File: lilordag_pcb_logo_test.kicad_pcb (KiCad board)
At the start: 2 copper layers, 98.1 x 100 mm, 124 parts, among them J1 USB4105-GF-A, Q1 MMBT3906, Q2 BC846, Q3 MMBT3906, Q4 BC846, Q5 BC846, Q6 BC846, SW1 PCM12SMTR

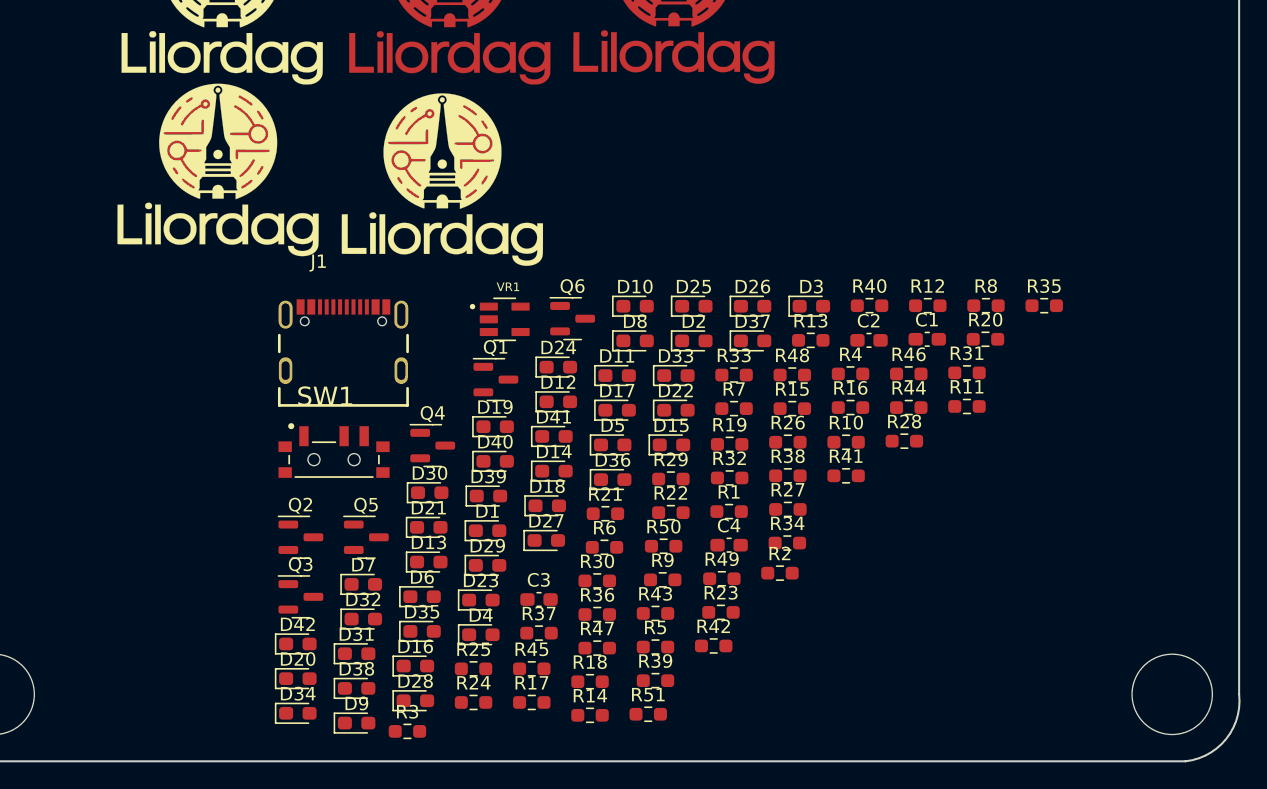
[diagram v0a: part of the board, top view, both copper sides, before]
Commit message: Added 2 CR2032 battery holders.
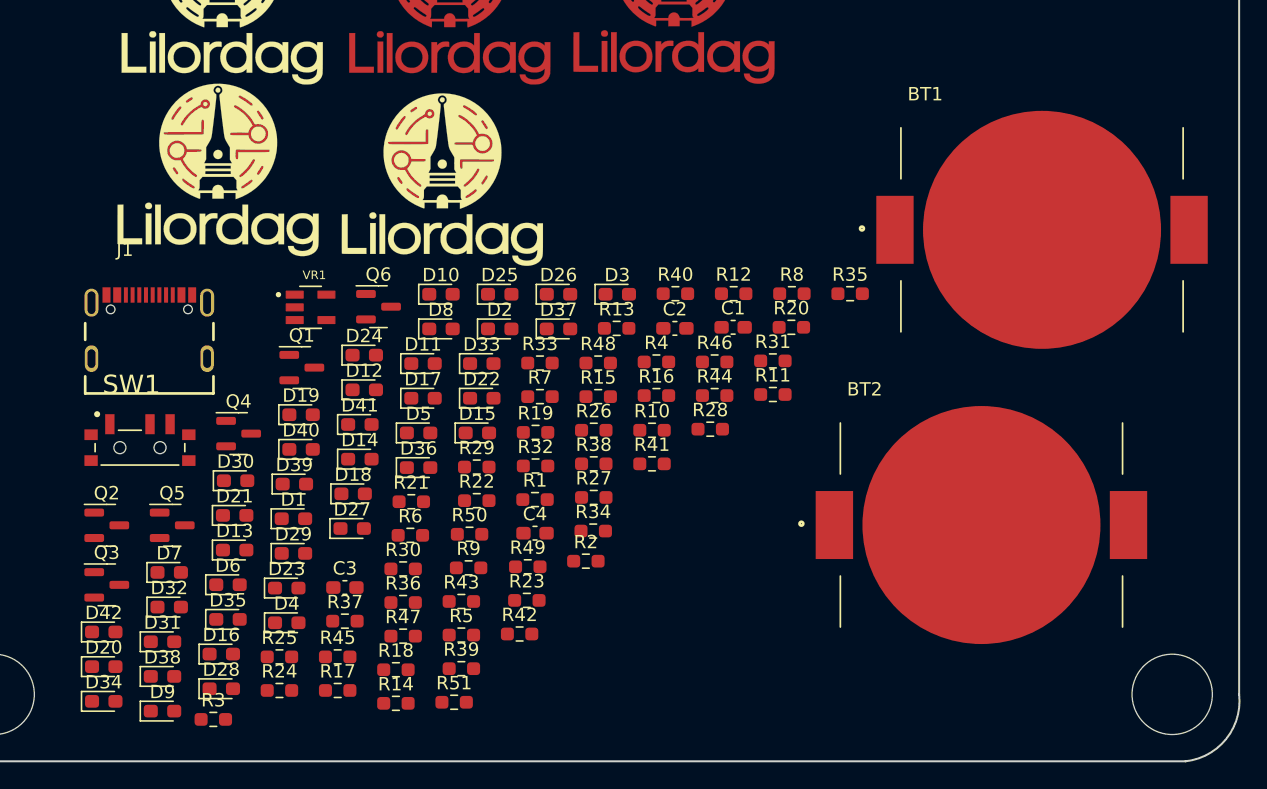
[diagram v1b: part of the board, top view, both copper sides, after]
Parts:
- added BT1: BK-912-TR, BK-912-TR-batt-holder:MPD_BK-912-TR, F.Cu at (111.3, 90.3)
- added BT2: BK-912-TR, BK-912-TR-batt-holder:MPD_BK-912-TR, F.Cu at (106.8, 112.3)
- moved D1 14.5 mm to (55.4, 111.9)
- moved D23 14.5 mm to (54.9, 117.1)
- moved D27 14.5 mm to (59.7, 112.6)
- moved D29 14.5 mm to (55.4, 114.5)
- moved D4 14.5 mm to (54.9, 119.7)
- moved Q1 14.5 mm to (56.0, 100.6)
- moved Q4 14.5 mm to (51.3, 105.5)
- moved R14 14.5 mm to (63.0, 125.7)
- moved R18 14.5 mm to (63.0, 123.2)
- moved VR1 14.5 mm to (56.6, 96.1)
- moved C1 14.5 mm to (88.2, 97.6)
- moved C2 14.5 mm to (83.8, 97.7)
- moved C3 14.5 mm to (59.2, 117.0)
- moved C4 14.5 mm to (73.4, 113.0)
- moved D10 14.5 mm to (66.4, 95.1)
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
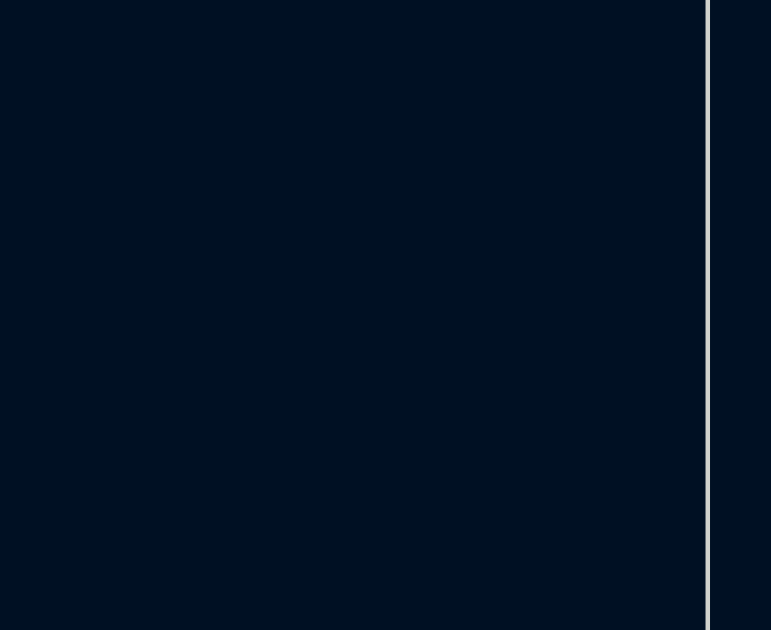
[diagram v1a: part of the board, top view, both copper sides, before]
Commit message: Added the protection circuit to the PCB.
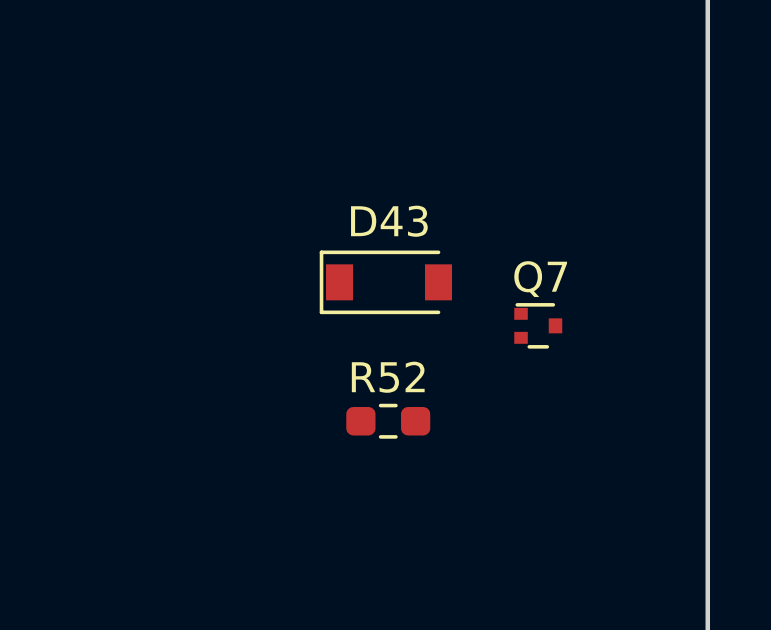
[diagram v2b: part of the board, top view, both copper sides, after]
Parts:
- added D43: MMSZ5233B 6V, Diode_SMD:D_SOD-123, F.Cu at (115.4, 65.8)
- added Q7: SSM3J56MFV, Package_TO_SOT_SMD:SOT-723, F.Cu at (120.3, 67.2)
- added R52: 100k, Resistor_SMD:R_0603_1608Metric_Pad0.98x0.95mm_HandSolder, F.Cu at (115.3, 70.4)

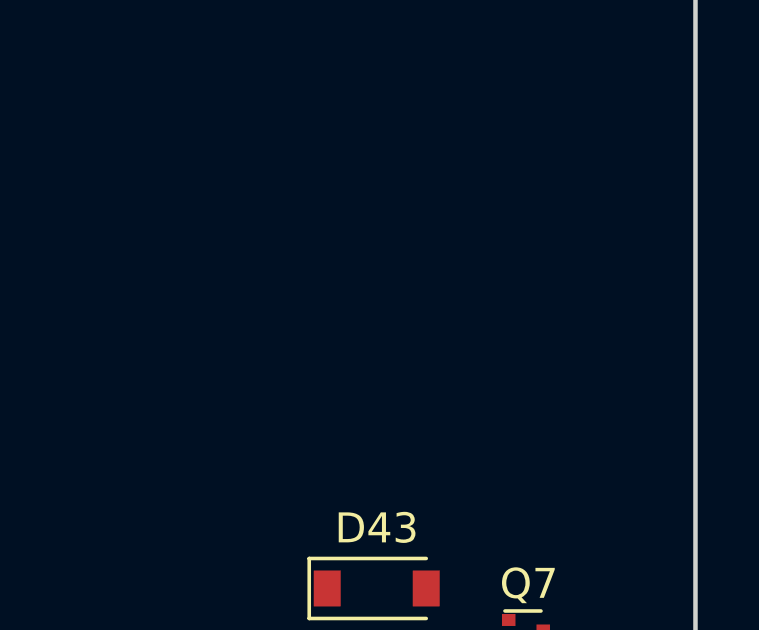
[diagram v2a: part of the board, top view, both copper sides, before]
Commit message: Added selector between battery and USB.
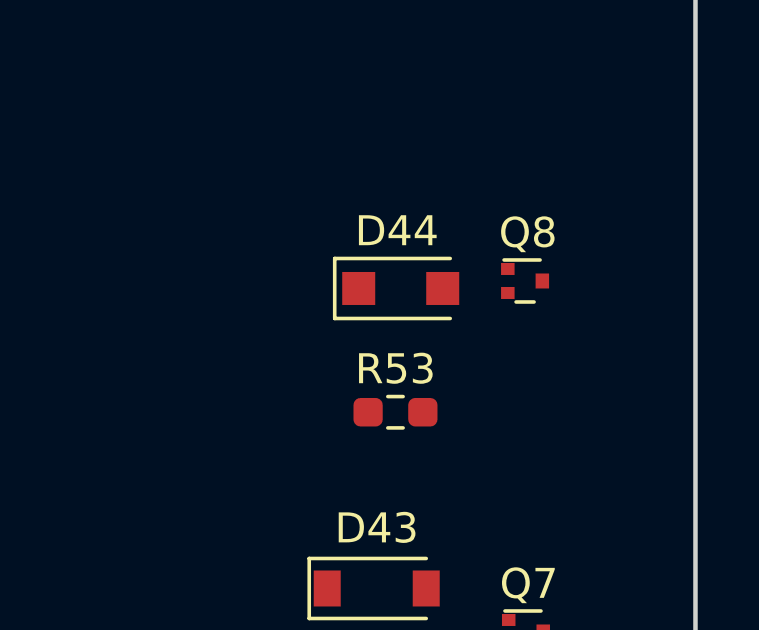
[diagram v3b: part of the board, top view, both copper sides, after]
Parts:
- added D44: D_Schottky, Diode_SMD:D_SOD-123F, F.Cu at (116.2, 55.8)
- added Q8: SSM3J56MFV, Package_TO_SOT_SMD:SOT-723, F.Cu at (120.3, 55.5)
- added R53: 100k, Resistor_SMD:R_0603_1608Metric_Pad0.98x0.95mm_HandSolder, F.Cu at (116.0, 59.9)

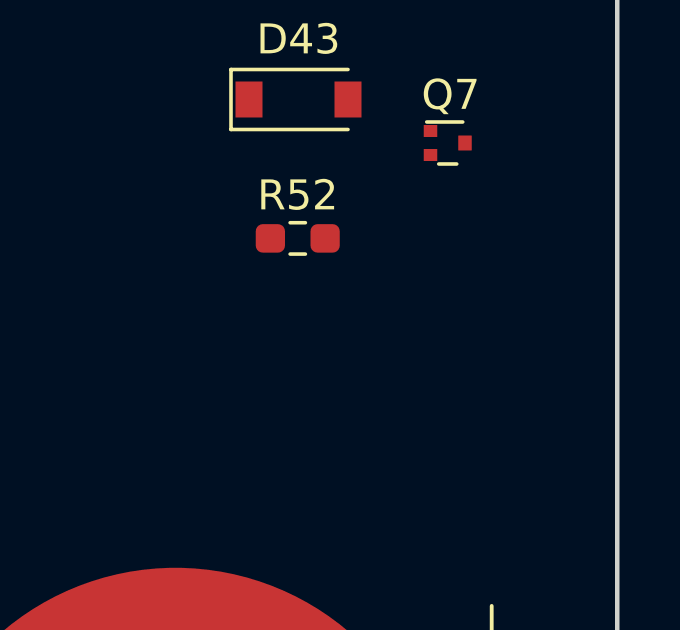
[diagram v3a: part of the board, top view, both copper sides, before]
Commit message: Added an on-off switch to the battery.
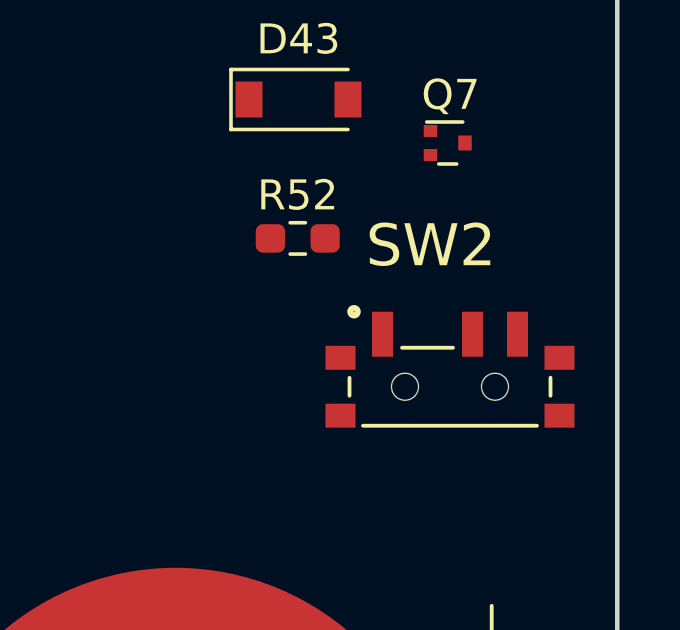
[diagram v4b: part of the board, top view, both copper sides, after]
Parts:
- added SW2: PCM12SMTR, PCM12SMTR:SW_PCM12SMTR, F.Cu at (120.4, 75.4)
- Q1: value MMBT3906 -> BC846
- Q4: value BC846 -> MMBT3906
- R1, R24, R25, R46: value 1k -> 470
- R10, R12, R31, R33: value 470 -> 1k
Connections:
- BT1 pad 1: +BATT -> Net-(BT1-Pad1)
- BT1 pad 2: +BATT -> Net-(BT1-Pad1)
- D1 pad 1: GND -> Net-(D1-Pad1)
- D10 pad 1: GND -> Net-(D10-Pad1)
- D11 pad 1: Net-(D11-Pad1) -> Net-(D1-Pad1)
- D12 pad 1: Net-(D11-Pad1) -> Net-(D10-Pad1)
- D13 pad 1: Net-(D11-Pad1) -> Net-(D1-Pad1)
- D14 pad 1: Net-(D11-Pad1) -> Net-(D10-Pad1)
- D15 pad 1: Net-(D11-Pad1) -> Net-(D1-Pad1)
- D16 pad 1: Net-(D11-Pad1) -> Net-(D10-Pad1)
- D17 pad 1: Net-(D11-Pad1) -> Net-(D1-Pad1)
- D18 pad 1: Net-(D11-Pad1) -> Net-(D10-Pad1)
- D19 pad 1: Net-(D11-Pad1) -> Net-(D1-Pad1)
- D2 pad 1: GND -> Net-(D10-Pad1)
- D20 pad 1: Net-(D11-Pad1) -> Net-(D10-Pad1)
- D21 pad 1: Net-(D21-Pad1) -> GND
- D22 pad 1: Net-(D21-Pad1) -> GND
- D23 pad 1: Net-(D21-Pad1) -> GND
- D24 pad 1: Net-(D21-Pad1) -> GND
- D25 pad 1: Net-(D21-Pad1) -> GND
- D26 pad 1: Net-(D21-Pad1) -> GND
- D27 pad 1: Net-(D21-Pad1) -> GND
- D28 pad 1: Net-(D21-Pad1) -> GND
- D29 pad 1: Net-(D21-Pad1) -> GND
- D3 pad 1: GND -> Net-(D1-Pad1)
- D30 pad 1: Net-(D21-Pad1) -> GND
- D4 pad 1: GND -> Net-(D10-Pad1)
- D5 pad 1: GND -> Net-(D1-Pad1)
- D6 pad 1: GND -> Net-(D10-Pad1)
- D7 pad 1: GND -> Net-(D1-Pad1)
- D8 pad 1: GND -> Net-(D10-Pad1)
- D9 pad 1: GND -> Net-(D1-Pad1)
- Q1 pad 2: +3.3V -> GND
- Q1 pad 3: Net-(Q1-Pad3) -> Net-(D1-Pad1)
- Q2 pad 3: Net-(D11-Pad1) -> Net-(D10-Pad1)
- Q4 pad 2: GND -> +3.3V
- Q4 pad 3: Net-(D21-Pad1) -> Net-(Q4-Pad3)
- R1 pad 1: LEFT_LED_CONNECTION -> +3.3V
- R1 pad 2: Net-(Q1-Pad1) -> Net-(D1-Pad2)
- R10 pad 1: Net-(Q1-Pad3) -> LEFT_LED_CONNECTION
- R10 pad 2: Net-(D7-Pad2) -> Net-(Q1-Pad1)
- R11 pad 1: Net-(Q1-Pad3) -> +3.3V
- R12 pad 1: Net-(Q1-Pad3) -> RIGHT_LED_CONNECTION
- R12 pad 2: Net-(D9-Pad2) -> Net-(Q2-Pad1)
- R13 pad 1: Net-(Q1-Pad3) -> +3.3V
- R13 pad 2: Net-(D10-Pad2) -> Net-(D9-Pad2)
- R14 pad 2: Net-(D11-Pad2) -> Net-(D10-Pad2)
- R15 pad 2: Net-(D12-Pad2) -> Net-(D11-Pad2)
- R16 pad 2: Net-(D13-Pad2) -> Net-(D12-Pad2)
- R17 pad 2: Net-(D14-Pad2) -> Net-(D13-Pad2)
- R18 pad 2: Net-(D15-Pad2) -> Net-(D14-Pad2)
- R19 pad 2: Net-(D16-Pad2) -> Net-(D15-Pad2)
- R20 pad 2: Net-(D17-Pad2) -> Net-(D16-Pad2)
- R21 pad 2: Net-(D18-Pad2) -> Net-(D17-Pad2)
- R22 pad 2: Net-(D19-Pad2) -> Net-(D18-Pad2)
- R23 pad 2: Net-(D20-Pad2) -> Net-(D19-Pad2)
- R24 pad 1: LEFT_LED_CONNECTION -> +3.3V
- R24 pad 2: Net-(Q2-Pad1) -> Net-(D20-Pad2)
- R25 pad 1: RIGHT_LED_CONNECTION -> Net-(Q3-Pad3)
- R25 pad 2: Net-(Q3-Pad1) -> Net-(D21-Pad2)
- R26 pad 1: +3.3V -> Net-(Q4-Pad3)
- R26 pad 2: Net-(D21-Pad2) -> Net-(D22-Pad2)
- R27 pad 1: +3.3V -> Net-(Q3-Pad3)
- R27 pad 2: Net-(D22-Pad2) -> Net-(D23-Pad2)
- R28 pad 1: +3.3V -> Net-(Q4-Pad3)
- R28 pad 2: Net-(D23-Pad2) -> Net-(D24-Pad2)
- R29 pad 1: +3.3V -> Net-(Q3-Pad3)
- R29 pad 2: Net-(D24-Pad2) -> Net-(D25-Pad2)
- R30 pad 1: +3.3V -> Net-(Q4-Pad3)
- R30 pad 2: Net-(D25-Pad2) -> Net-(D26-Pad2)
- R31 pad 1: +3.3V -> LEFT_LED_CONNECTION
- R31 pad 2: Net-(D26-Pad2) -> Net-(Q3-Pad1)
- R32 pad 1: +3.3V -> Net-(Q3-Pad3)
- R33 pad 1: +3.3V -> RIGHT_LED_CONNECTION
- R33 pad 2: Net-(D28-Pad2) -> Net-(Q4-Pad1)
- R34 pad 1: +3.3V -> Net-(Q4-Pad3)
- R34 pad 2: Net-(D29-Pad2) -> Net-(D28-Pad2)
- R35 pad 1: +3.3V -> Net-(Q3-Pad3)
- R35 pad 2: Net-(D30-Pad2) -> Net-(D29-Pad2)
- R36 pad 1: Net-(Q3-Pad3) -> Net-(Q4-Pad3)
- R36 pad 2: Net-(D31-Pad2) -> Net-(D30-Pad2)
- R37 pad 2: Net-(D32-Pad2) -> Net-(D31-Pad2)
- R38 pad 1: Net-(Q3-Pad3) -> Net-(Q4-Pad3)
- R38 pad 2: Net-(D33-Pad2) -> Net-(D32-Pad2)
- R39 pad 2: Net-(D34-Pad2) -> Net-(D33-Pad2)
- R4 pad 1: Net-(Q1-Pad3) -> +3.3V
- R4 pad 2: Net-(D1-Pad2) -> Net-(D2-Pad2)
- R40 pad 1: Net-(Q3-Pad3) -> Net-(Q4-Pad3)
- R40 pad 2: Net-(D35-Pad2) -> Net-(D34-Pad2)
- R41 pad 2: Net-(D36-Pad2) -> Net-(D35-Pad2)
- R42 pad 1: Net-(Q3-Pad3) -> Net-(Q4-Pad3)
- R42 pad 2: Net-(D37-Pad2) -> Net-(D36-Pad2)
- R43 pad 2: Net-(D38-Pad2) -> Net-(D37-Pad2)
- R44 pad 1: Net-(Q3-Pad3) -> Net-(Q4-Pad3)
- R44 pad 2: Net-(D39-Pad2) -> Net-(D38-Pad2)
- R45 pad 2: Net-(D40-Pad2) -> Net-(D39-Pad2)
- R46 pad 1: RIGHT_LED_CONNECTION -> Net-(Q4-Pad3)
- R46 pad 2: Net-(Q4-Pad1) -> Net-(D40-Pad2)
- R5 pad 1: Net-(Q1-Pad3) -> +3.3V
- R5 pad 2: Net-(D2-Pad2) -> Net-(D3-Pad2)
- R6 pad 1: Net-(Q1-Pad3) -> +3.3V
- R6 pad 2: Net-(D3-Pad2) -> Net-(D4-Pad2)
- R7 pad 1: Net-(Q1-Pad3) -> +3.3V
- R7 pad 2: Net-(D4-Pad2) -> Net-(D5-Pad2)
- R8 pad 1: Net-(Q1-Pad3) -> +3.3V
- R8 pad 2: Net-(D5-Pad2) -> Net-(D6-Pad2)
- R9 pad 1: Net-(Q1-Pad3) -> +3.3V
- R9 pad 2: Net-(D6-Pad2) -> Net-(D7-Pad2)

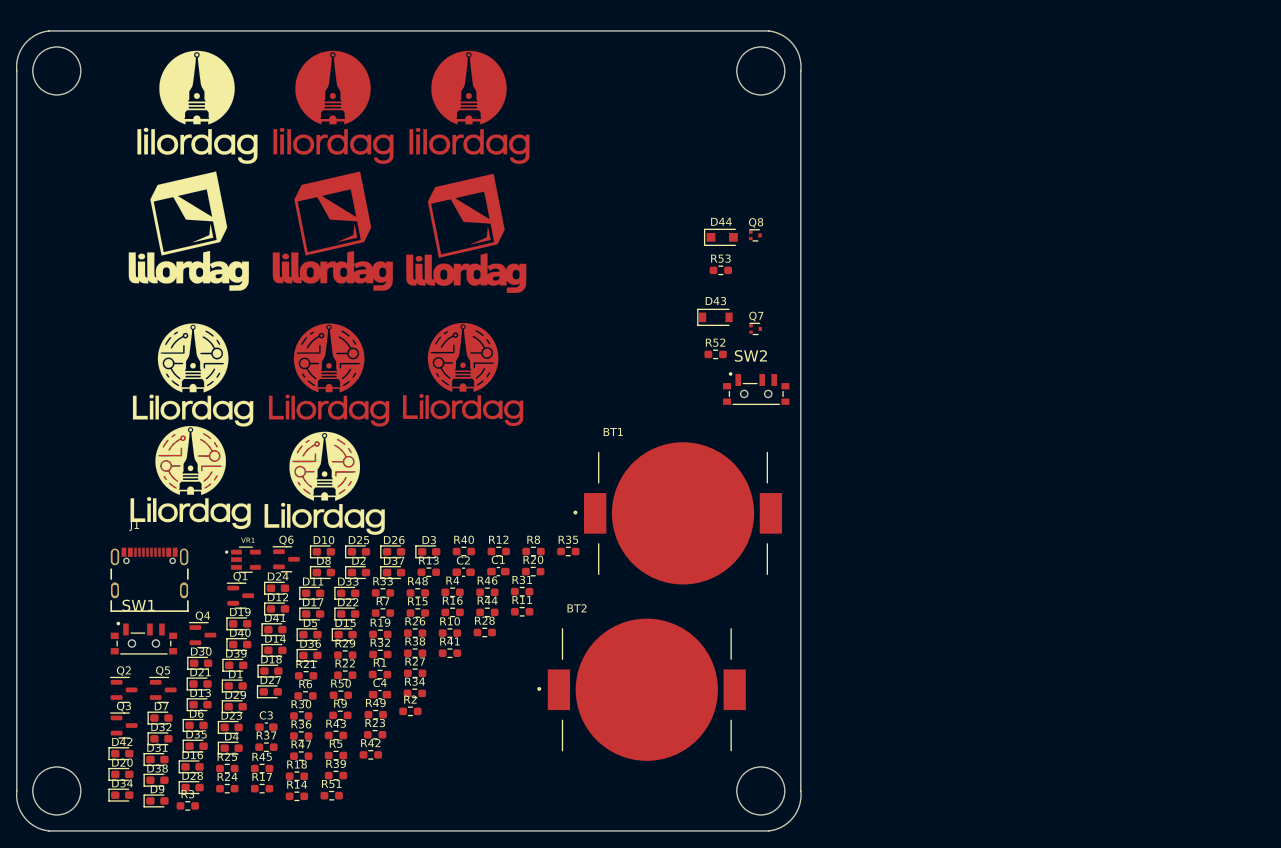
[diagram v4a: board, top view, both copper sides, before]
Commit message: Added datasheet for the LED and assigned 3d parts.
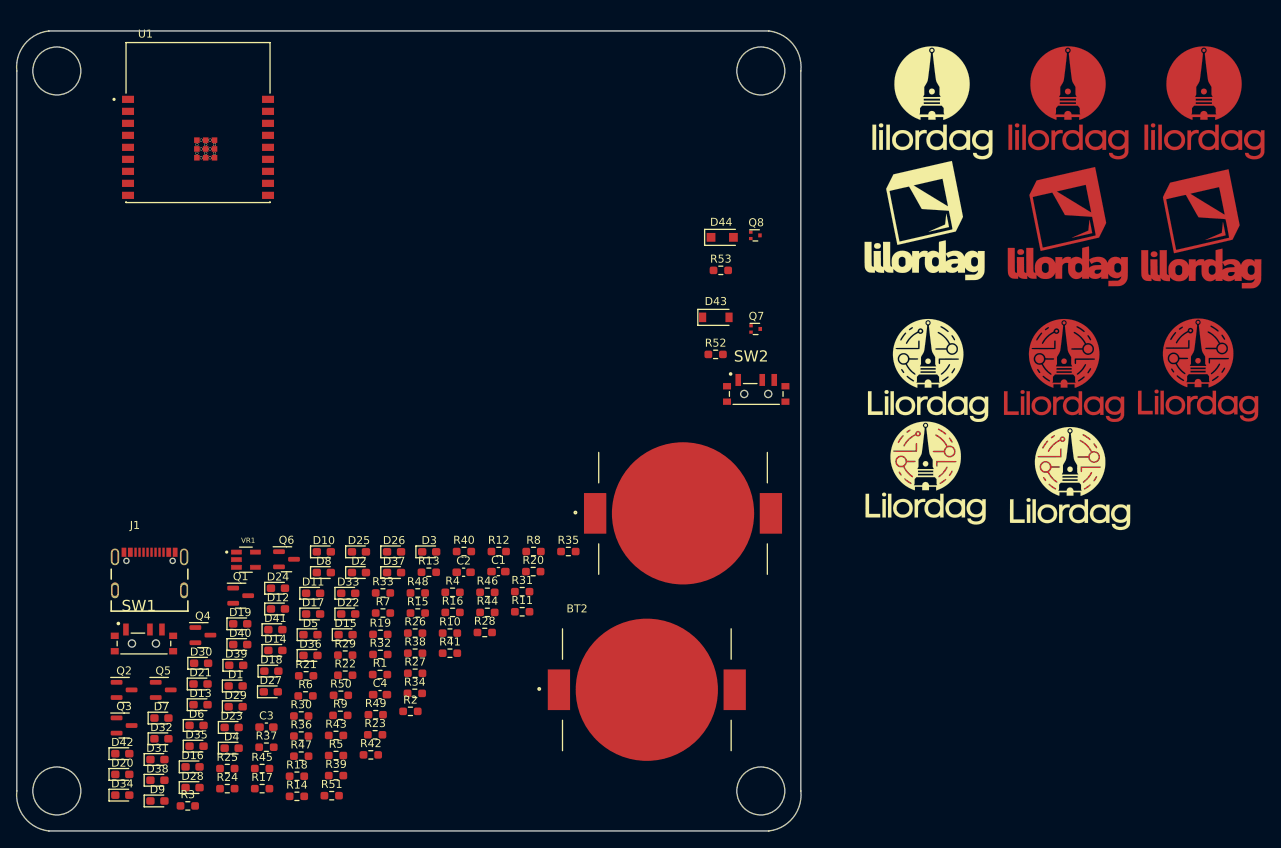
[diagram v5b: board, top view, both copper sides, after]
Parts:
- added U1: ESP32-C3-WROOM-02-N4, ESP32-C3-WROOM:MODULE_ESP32-C3-WROOM-02-H4, F.Cu at (50.6, 41.5)
- moved Ref** 93.2 mm to (160.7, 85.0)
- moved Ref** 92.0 mm to (147.8, 60.6)
- moved Ref** 91.9 mm to (142.7, 71.4)
- moved Ref** 91.9 mm to (142.6, 84.3)
- moved Ref** 91.9 mm to (147.7, 44.3)
- moved Ref** 91.9 mm to (165.7, 61.3)
- moved Ref** 91.9 mm to (193.7, 71.4)
- moved Ref** 91.9 mm to (159.7, 71.4)
- moved Ref** 91.9 mm to (198.7, 44.3)
- moved Ref** 91.9 mm to (198.7, 61.3)
- moved Ref** 91.9 mm to (164.7, 44.3)
- moved Ref** 91.9 mm to (181.7, 44.3)
- moved Ref** 91.9 mm to (176.7, 71.4)
- moved Ref** 91.9 mm to (182.7, 61.3)
